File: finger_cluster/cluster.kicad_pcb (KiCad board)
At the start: 2 copper layers, 43.1 x 61 mm, 16 parts, among them J1 Conn_01x06_MountingPin, Q1 BSS84, SW1 SW_SPST, U1 TMAG5263

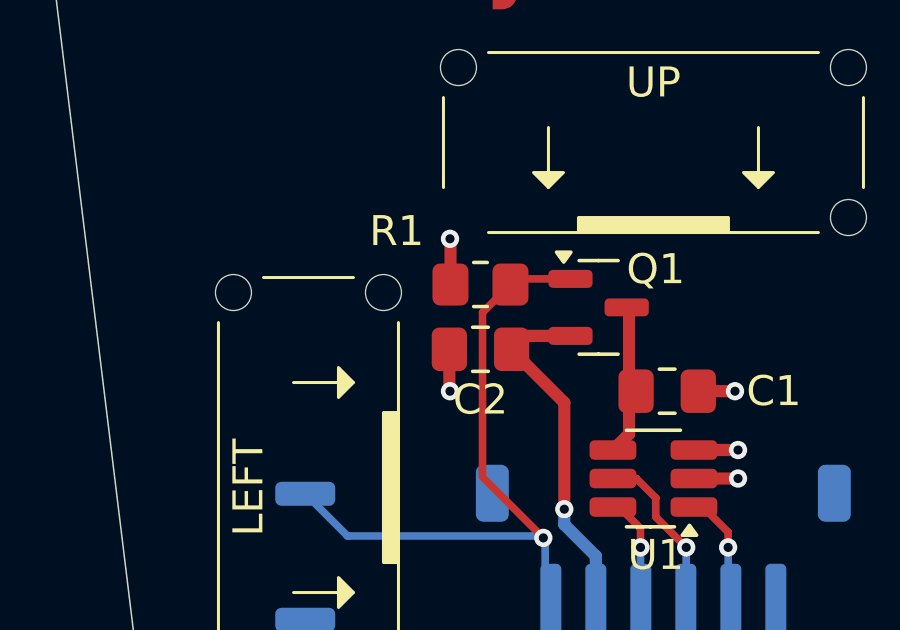
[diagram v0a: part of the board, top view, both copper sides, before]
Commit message: cluster key resizes
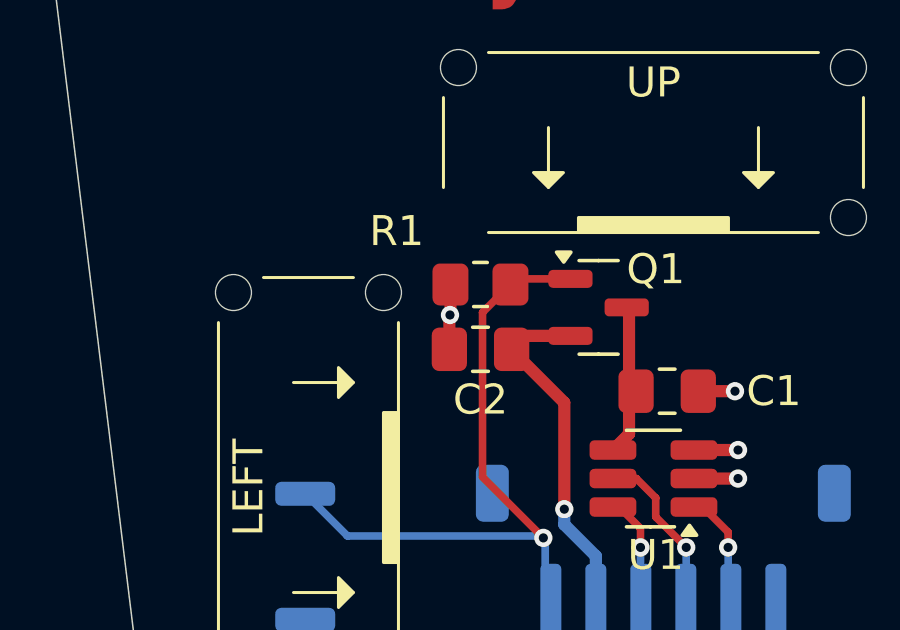
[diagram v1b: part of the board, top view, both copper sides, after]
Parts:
- moved REF** 0.75 mm to (85.1, 40.7)
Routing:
- net GND: track 7.10 -> 6.34 mm, vias 5 -> 4
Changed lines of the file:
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@@
 	(footprint "Symbol:OSHW-Symbol_8.9x8mm_SilkScreen"
 		(layer "B.Cu")
-		(at 85 40 180)
+		(at 85.09 40.7416 180)
 		(descr "Open Source Hardware Symbol")
 		(tags "Logo Symbol OSHW")
@@
 		)
 	)
+	(gr_circle
+		(center 100 50)
+		(end 105 50)
+		(stroke
+			(width 0.2)
+			(type solid)
+		)
+		(fill no)
+		(layer "Cmts.User")
+	)
 	(gr_line
 		(start 84 96)
@@
 	)
 	(segment
-		(start 93.1965 75.692)
-		(end 93.1965 77.0675)
-		(width 0.4064)
-		(layer "F.Cu")
-		(net 1)
-	)
-	(segment
-		(start 93.234 72.025)
-		(end 93.218 72.009)
+		(start 93.218 74.549)
+		(end 93.234 74.533)
 		(width 0.4064)
 		(layer "F.Cu")
@@
 	)
 	(segment
+		(start 93.1965 74.5705)
+		(end 93.1965 75.692)
+		(width 0.4064)
+		(layer "F.Cu")
+		(net 1)
+	)
+	(segment
 		(start 102.8192 79.05)
 		(end 101.35 79.05)
@@
 	)
 	(segment
-		(start 93.234 73.533)
-		(end 93.234 72.025)
-		(width 0.4064)
-		(layer "F.Cu")
-		(net 1)
-	)
-	(segment
-		(start 93.1965 77.0675)
-		(end 93.218 77.089)
+		(start 93.234 74.533)
+		(end 93.234 73.533)
 		(width 0.4064)
 		(layer "F.Cu")
@@
 		(net 1)
 	)
+	(segment
+		(start 93.218 74.549)
+		(end 93.1965 74.5705)
+		(width 0.4064)
+		(layer "F.Cu")
+		(net 1)
+	)
 	(via
 		(at 102.8192 80)
@@
 	)
 	(via
-		(at 93.218 77.089)
+		(at 93.218 74.549)
 		(size 0.6096)
 		(drill 0.3048)
-		(layers "F.Cu" "B.Cu")
-		(net 1)
-	)
-	(via
-		(at 93.218 72.009)
-		(size 0.6096)
-		(drill 0.3048)

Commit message: aaa
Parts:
- moved UP 3.80 mm to (100.0, 63.0)
- moved LEFT 2.75 mm to (85.0, 78.0)
- moved RIGHT 2.75 mm to (115.0, 78.0)
- moved J1 2.32 mm to (100.2, 80.2)
- moved Q1 2.32 mm to (98.0, 72.0)
- moved R1 2.32 mm to (94.1, 71.2)
- moved C1 2.32 mm to (100.3, 74.8)
- moved C2 2.32 mm to (94.1, 73.4)
- moved SW1 2.32 mm to (88.2, 80.3)
- moved U1 2.30 mm to (100.0, 77.7)
- moved DOWN 0.80 mm to (100.0, 93.0)

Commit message: cluster aluminium basic
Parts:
- removed DOWN, LEFT, RIGHT, UP: key, cluster:key
- added H5: MountingHole_Pad, MountingHole:MountingHole_3.2mm_M3_DIN965_Pad, F.Cu at (187.5, 55.0)
- added REF**: key, cluster:key, F.Cu at (172.5, 77.5)
- added REF**: key, cluster:key, F.Cu at (187.5, 92.5)
- added REF**: key, cluster:key, F.Cu at (202.5, 77.5)
- added REF**: key, cluster:key, F.Cu at (187.5, 62.5)
- H1, H2: footprint MountingHole:MountingHole_5.3mm_M5_ISO14580_Pad -> MountingHole:MountingHole_2.7mm_M2.5_DIN965_Pad
- SW1: moved to F.Cu
- moved REF** 114.7 mm to (198.9, 55.4)
- moved H2 98.7 mm to (173.5, 91.5), turned to 180 degrees
- moved R1 95.9 mm to (190.0, 70.1), turned to 0 degrees
- moved H1 95.0 mm to (201.5, 91.5), turned to 180 degrees
- moved H4 93.2 mm to (175.5, 64.5), turned to 180 degrees
- moved H3 90.8 mm to (199.5, 64.5), turned to 180 degrees
- moved SW1 90.4 mm to (175.0, 55.0), turned to 180 degrees
- moved U1 87.5 mm to (187.5, 77.5)
- moved Q1 87.5 mm to (185.5, 71.1)
- moved J1 87.4 mm to (187.5, 83.5)
- moved C2 87.3 mm to (181.4, 72.1)
- moved C1 87.1 mm to (187.5, 74.4)
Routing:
- net /RST: track 22.6 -> 39.5 mm
- net +3.3V: track 23.6 -> 37.1 mm
- net /INT': track 5.67 -> 8.98 mm
- net /SDA: track 3.75 -> 6.95 mm
- net /SCL: track 3.93 -> 7.07 mm
- net GND: track 6.34 -> 7.39 mm, vias 4 -> 5
- net VDD: track 5.01 -> 5.95 mm
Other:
- board size 43.1 x 61 mm -> 35 x 45.5 mm
- board text added: "yadh2-2"
- board text removed: "JLCJLCJLCJLC"
- board text removed: "yadh2-1"
